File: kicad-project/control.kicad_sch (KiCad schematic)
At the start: 34 parts, among them J1 Conn_02x04_Counter_Clockwise, J2 Conn_02x08_Counter_Clockwise, SW1 HOME_SW, SW2 EN_SW, SW3 PRG_SW, SW4 RST_SW, U1 W25Q16JVSS, U2 RP2040, Y1 12MHz

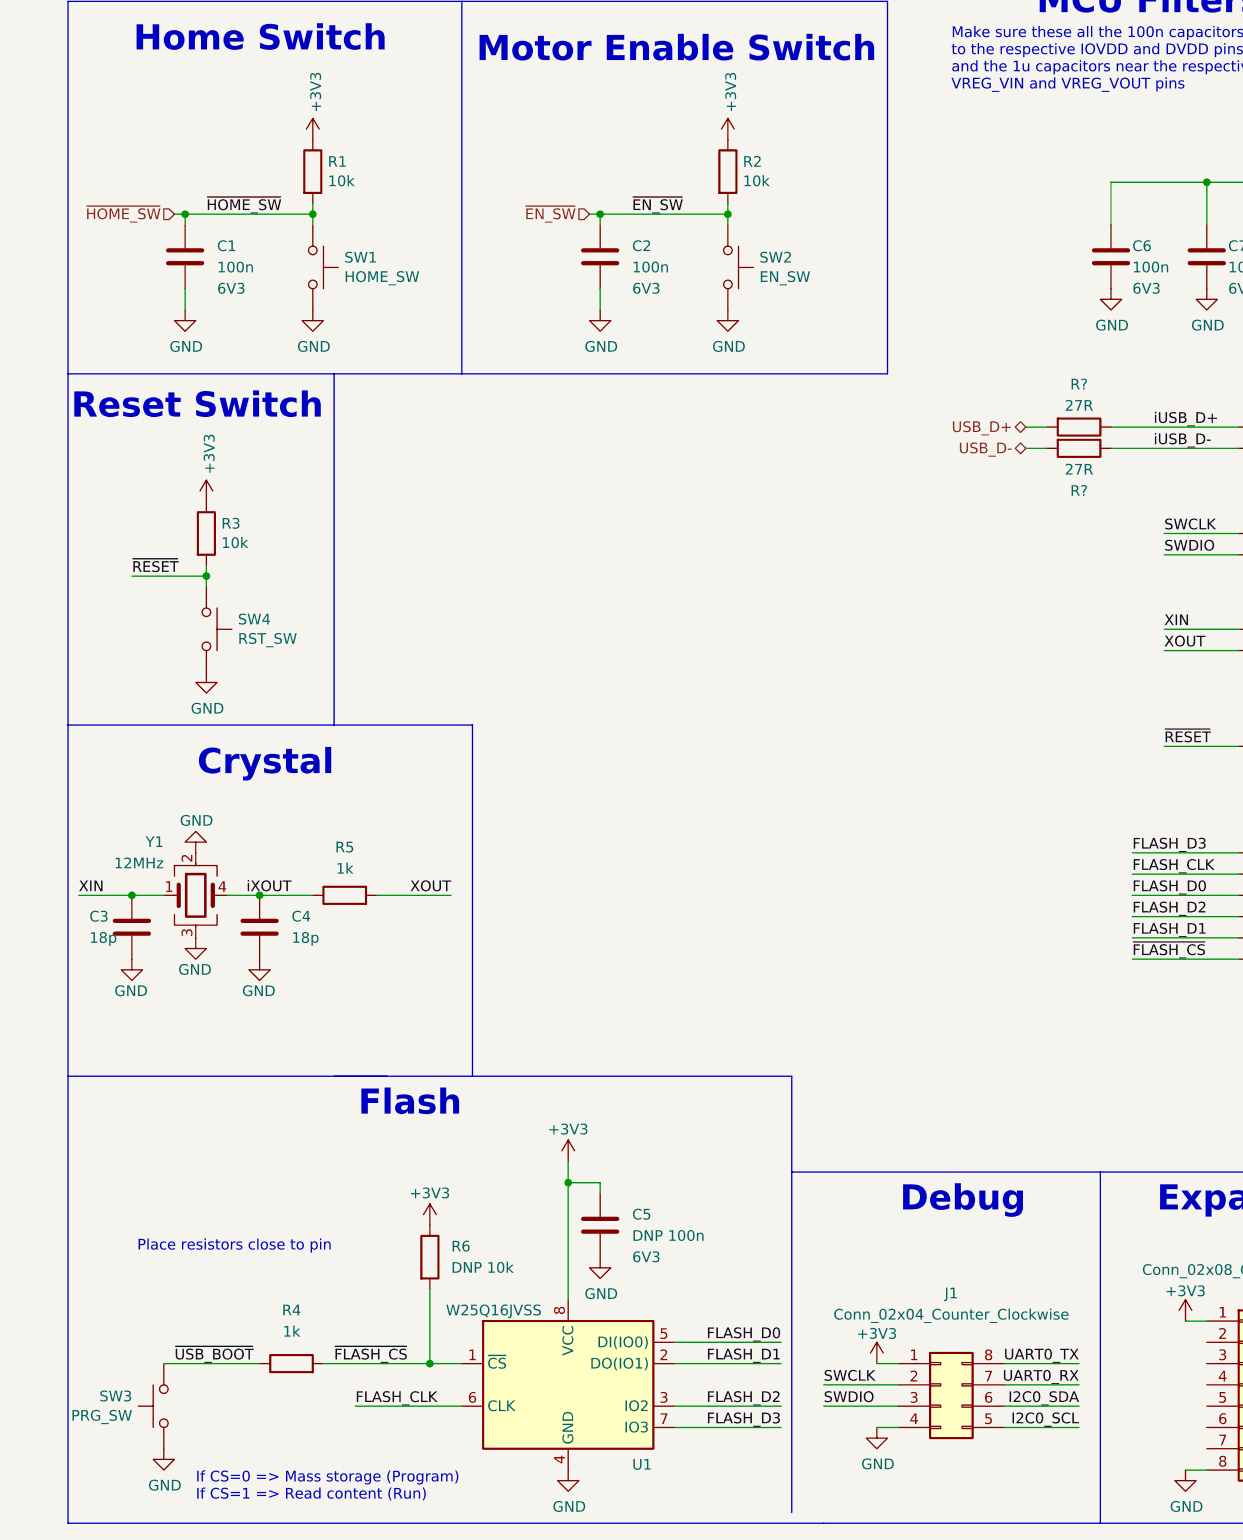
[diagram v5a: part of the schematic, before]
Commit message: hw: add mounting holes
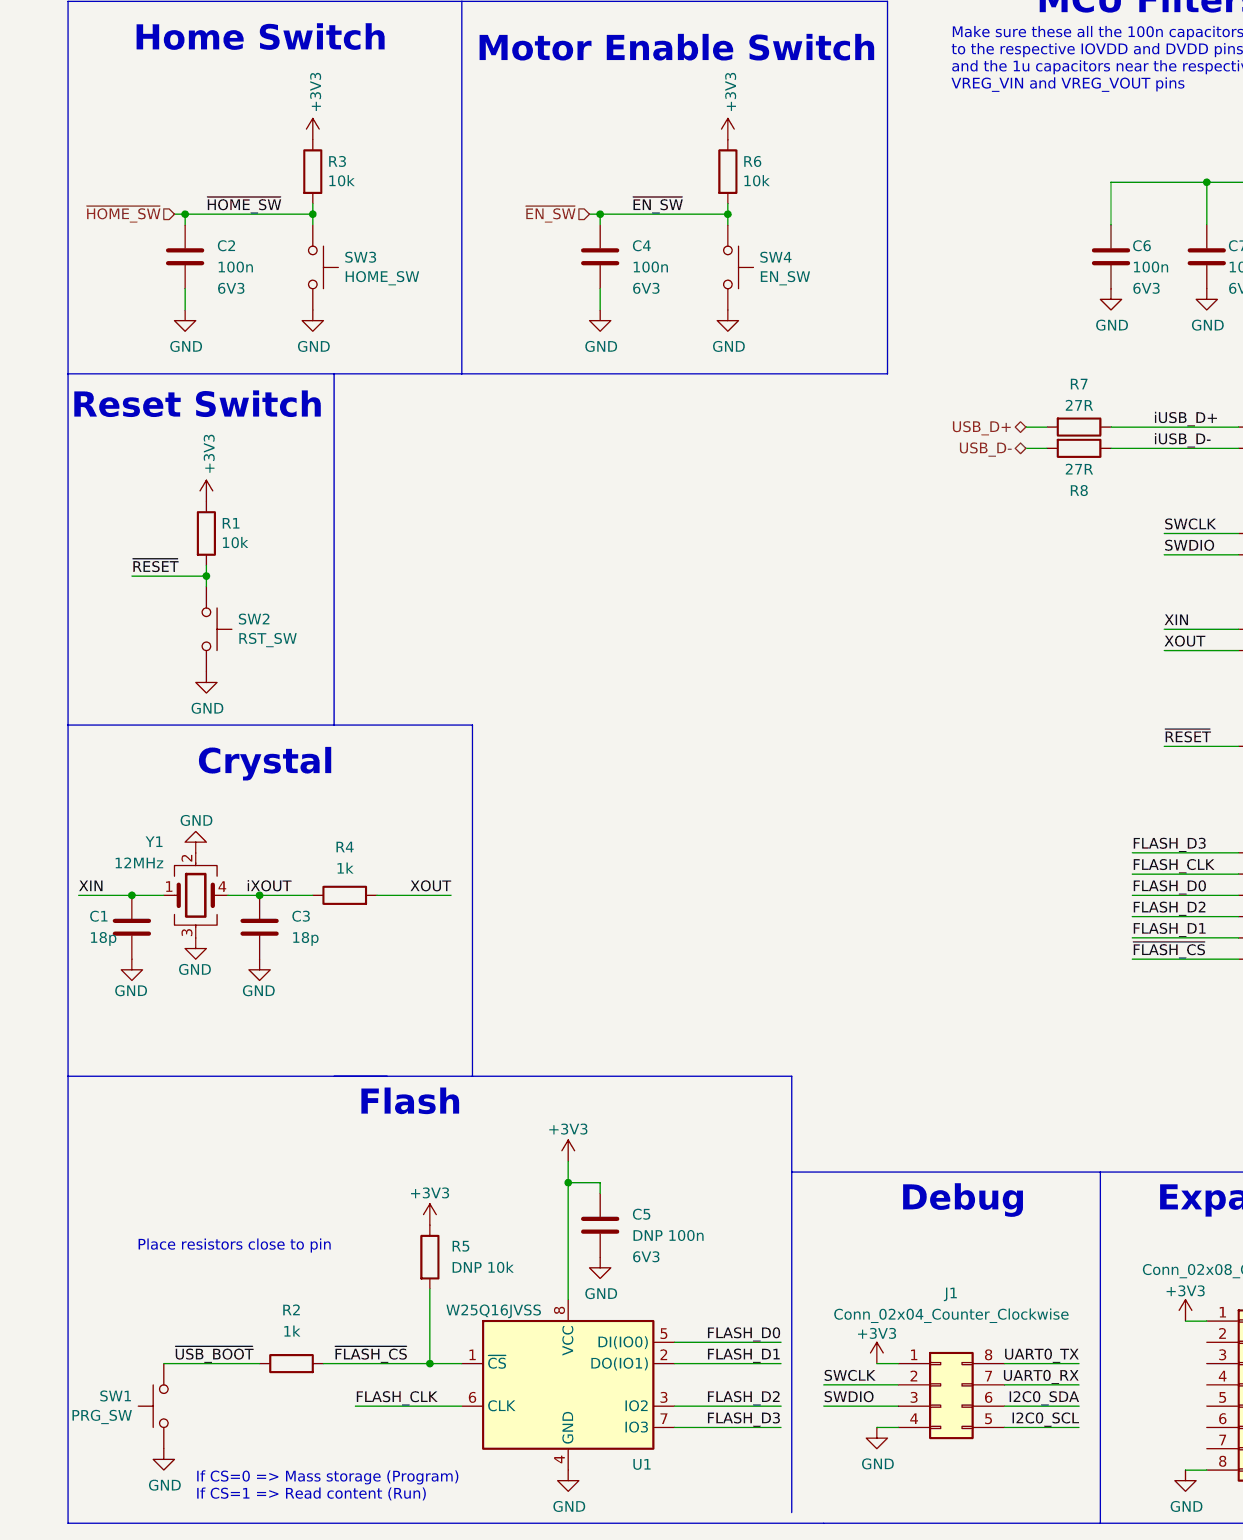
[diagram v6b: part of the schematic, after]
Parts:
- gave numbers to parts that had none: 2
- renumbered C3 to C1, C1 to C2, C4 to C3, C2 to C4, R3 to R1, R4 to R2, R1 to R3, R5 to R4, R6 to R5, R2 to R6, SW3 to SW1, SW4 to SW2, SW1 to SW3, SW2 to SW4
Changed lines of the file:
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@@
   (symbol (lib_id "Switch:SW_Push") (at 29.21 90.17 270) (unit 1)
     (in_bom yes) (on_board yes)
-    (property "Reference" "SW4" (id 0) (at 32.9692 89.0016 90)
+    (property "Reference" "SW2" (id 0) (at 32.9692 89.0016 90)
       (effects (font (size 1.27 1.27)) (justify left))
     )
@@
   (symbol (lib_id "Device:R") (at 29.21 78.74 0) (unit 1)
     (in_bom yes) (on_board yes)
-    (property "Reference" "R3" (id 0) (at 30.988 77.5716 0)
+    (property "Reference" "R1" (id 0) (at 30.988 77.5716 0)
       (effects (font (size 1.27 1.27)) (justify left))
     )
@@
   (symbol (lib_id "power:GND") (at 29.21 95.25 0) (unit 1)
     (in_bom yes) (on_board yes)
-    (property "Reference" "#PWR012" (id 0) (at 29.21 101.6 0)
+    (property "Reference" "#PWR07" (id 0) (at 29.21 101.6 0)
       (effects (font (size 1.27 1.27)) hide)
     )
@@
   (symbol (lib_id "power:+3V3") (at 29.21 74.93 0) (unit 1)
     (in_bom yes) (on_board yes)
-    (property "Reference" "#PWR011" (id 0) (at 29.21 78.74 0)
+    (property "Reference" "#PWR06" (id 0) (at 29.21 78.74 0)
       (effects (font (size 1.27 1.27)) hide)
     )
@@
   (symbol (lib_id "Device:R") (at 133.35 66.04 270) (unit 1)
     (in_bom yes) (on_board yes)
-    (property "Reference" "R?" (id 0) (at 133.35 60.96 90))
+    (property "Reference" "R7" (id 0) (at 133.35 60.96 90))
     (property "Value" "27R" (id 1) (at 133.35 63.5 90))
     (property "Footprint" "Resistor_SMD:R_0603_1608Metric" (id 2) (at 133.35 64.262 90)
@@
   (symbol (lib_id "Device:R") (at 133.35 68.58 270) (unit 1)
     (in_bom yes) (on_board yes)
-    (property "Reference" "R?" (id 0) (at 133.35 73.66 90))
+    (property "Reference" "R8" (id 0) (at 133.35 73.66 90))
     (property "Value" "27R" (id 1) (at 133.35 71.12 90))
     (property "Footprint" "Resistor_SMD:R_0603_1608Metric" (id 2) (at 133.35 66.802 90)
@@
   (symbol (lib_id "power:GND") (at 27.94 127 0) (unit 1)
     (in_bom yes) (on_board yes)
-    (property "Reference" "#PWR010" (id 0) (at 27.94 133.35 0)
+    (property "Reference" "#PWR05" (id 0) (at 27.94 133.35 0)
       (effects (font (size 1.27 1.27)) hide)
     )
@@
   (symbol (lib_id "power:GND") (at 27.94 116.84 180) (unit 1)
     (in_bom yes) (on_board yes)
-    (property "Reference" "#PWR09" (id 0) (at 27.94 110.49 0)
+    (property "Reference" "#PWR04" (id 0) (at 27.94 110.49 0)
       (effects (font (size 1.27 1.27)) hide)
     )
@@
   (symbol (lib_id "power:+3V3") (at 55.88 161.29 0) (unit 1)
     (in_bom yes) (on_board yes)
-    (property "Reference" "#PWR014" (id 0) (at 55.88 165.1 0)
+    (property "Reference" "#PWR011" (id 0) (at 55.88 165.1 0)
       (effects (font (size 1.27 1.27)) hide)
     )
@@
   (symbol (lib_id "Device:R") (at 91.44 35.56 0) (unit 1)
     (in_bom yes) (on_board yes)
-    (property "Reference" "R2" (id 0) (at 93.218 34.3916 0)
+    (property "Reference" "R6" (id 0) (at 93.218 34.3916 0)
       (effects (font (size 1.27 1.27)) (justify left))
     )
@@
   (symbol (lib_id "power:GND") (at 24.13 187.96 0) (unit 1)
     (in_bom yes) (on_board yes)
-    (property "Reference" "#PWR08" (id 0) (at 24.13 194.31 0)
+    (property "Reference" "#PWR02" (id 0) (at 24.13 194.31 0)
       (effects (font (size 1.27 1.27)) hide)
     )
@@
   (symbol (lib_id "Switch:SW_Push") (at 91.44 46.99 270) (unit 1)
     (in_bom yes) (on_board yes)
-    (property "Reference" "SW2" (id 0) (at 95.1992 45.8216 90)
+    (property "Reference" "SW4" (id 0) (at 95.1992 45.8216 90)
       (effects (font (size 1.27 1.27)) (justify left))
     )
@@
   (symbol (lib_id "Switch:SW_Push") (at 24.13 182.88 90) (mirror x) (unit 1)
     (in_bom yes) (on_board yes)
-    (property "Reference" "SW3" (id 0) (at 20.3708 181.7116 90)
+    (property "Reference" "SW1" (id 0) (at 20.3708 181.7116 90)
       (effects (font (size 1.27 1.27)) (justify left))
     )
@@
   (symbol (lib_id "power:GND") (at 76.2 165.1 0) (unit 1)
     (in_bom yes) (on_board yes)
-    (property "Reference" "#PWR017" (id 0) (at 76.2 171.45 0)
+    (property "Reference" "#PWR015" (id 0) (at 76.2 171.45 0)
       (effects (font (size 1.27 1.27)) hide)
     )
@@
   (symbol (lib_id "Device:C") (at 76.2 45.72 0) (unit 1)
     (in_bom yes) (on_board yes)
-    (property "Reference" "C2" (id 0) (at 80.01 44.4499 0)
+    (property "Reference" "C4" (id 0) (at 80.01 44.4499 0)
       (effects (font (size 1.27 1.27)) (justify left))
     )
@@
   (symbol (lib_id "Device:C") (at 20.32 125.73 0) (unit 1)
     (in_bom yes) (on_board yes)
-    (property "Reference" "C3" (id 0) (at 15.24 124.46 0)
+    (property "Reference" "C1" (id 0) (at 15.24 124.46 0)
       (effects (font (size 1.27 1.27)) (justify left))
     )
@@
   (symbol (lib_id "Device:C") (at 26.67 45.72 0) (unit 1)
     (in_bom yes) (on_board yes)
-    (property "Reference" "C1" (id 0) (at 30.48 44.4499 0)
+    (property "Reference" "C2" (id 0) (at 30.48 44.4499 0)
       (effects (font (size 1.27 1.27)) (justify left))
     )
@@
   (symbol (lib_id "Device:C") (at 35.56 125.73 0) (unit 1)
     (in_bom yes) (on_board yes) (fields_autoplaced)
-    (property "Reference" "C4" (id 0) (at 39.37 124.4599 0)
+    (property "Reference" "C3" (id 0) (at 39.37 124.4599 0)
       (effects (font (size 1.27 1.27)) (justify left))
     )
@@
   (symbol (lib_id "Device:R") (at 39.37 177.8 90) (unit 1)
     (in_bom yes) (on_board yes) (fields_autoplaced)
-    (property "Reference" "R4" (id 0) (at 39.37 171.45 90))
+    (property "Reference" "R2" (id 0) (at 39.37 171.45 90))
     (property "Value" "1k" (id 1) (at 39.37 173.99 90))
     (property "Footprint" "Resistor_SMD:R_0603_1608Metric" (id 2) (at 39.37 179.578 90)
@@
   (symbol (lib_id "power:GND") (at 41.91 52.07 0) (unit 1)
     (in_bom yes) (on_board yes)
-    (property "Reference" "#PWR03" (id 0) (at 41.91 58.42 0)
+    (property "Reference" "#PWR010" (id 0) (at 41.91 58.42 0)
       (effects (font (size 1.27 1.27)) hide)
     )
@@
   (symbol (lib_id "Switch:SW_Push") (at 41.91 46.99 270) (unit 1)
     (in_bom yes) (on_board yes)
-    (property "Reference" "SW1" (id 0) (at 45.6692 45.8216 90)
+    (property "Reference" "SW3" (id 0) (at 45.6692 45.8216 90)
       (effects (font (size 1.27 1.27)) (justify left))
     )
@@
   (symbol (lib_id "power:+3V3") (at 41.91 31.75 0) (unit 1)
     (in_bom yes) (on_board yes)
-    (property "Reference" "#PWR02" (id 0) (at 41.91 35.56 0)
+    (property "Reference" "#PWR09" (id 0) (at 41.91 35.56 0)
       (effects (font (size 1.27 1.27)) hide)
     )
@@
   (symbol (lib_id "Device:R") (at 41.91 35.56 0) (unit 1)
     (in_bom yes) (on_board yes)
-    (property "Reference" "R1" (id 0) (at 43.688 34.3916 0)
+    (property "Reference" "R3" (id 0) (at 43.688 34.3916 0)
       (effects (font (size 1.27 1.27)) (justify left))
     )
@@
   (symbol (lib_id "power:GND") (at 72.39 190.5 0) (unit 1)
     (in_bom yes) (on_board yes)
-    (property "Reference" "#PWR016" (id 0) (at 72.39 196.85 0)
+    (property "Reference" "#PWR013" (id 0) (at 72.39 196.85 0)
       (effects (font (size 1.27 1.27)) hide)
     )
@@
   (symbol (lib_id "power:GND") (at 26.67 52.07 0) (unit 1)
     (in_bom yes) (on_board yes)
-    (property "Reference" "#PWR01" (id 0) (at 26.67 58.42 0)
+    (property "Reference" "#PWR03" (id 0) (at 26.67 58.42 0)
       (effects (font (size 1.27 1.27)) hide)
     )
@@
   (symbol (lib_id "Device:R") (at 45.72 121.92 90) (unit 1)
     (in_bom yes) (on_board yes) (fields_autoplaced)
-    (property "Reference" "R5" (id 0) (at 45.72 116.205 90))
+    (property "Reference" "R4" (id 0) (at 45.72 116.205 90))
     (property "Value" "1k" (id 1) (at 45.72 118.745 90))
     (property "Footprint" "Resistor_SMD:R_0603_1608Metric" (id 2) (at 45.72 123.698 90)
@@
   (symbol (lib_id "power:GND") (at 20.32 129.54 0) (unit 1)
     (in_bom yes) (on_board yes)
-    (property "Reference" "#PWR07" (id 0) (at 20.32 135.89 0)
+    (property "Reference" "#PWR01" (id 0) (at 20.32 135.89 0)
       (effects (font (size 1.27 1.27)) hide)
     )
@@
   (symbol (lib_id "power:GND") (at 91.44 52.07 0) (unit 1)
     (in_bom yes) (on_board yes)
-    (property "Reference" "#PWR06" (id 0) (at 91.44 58.42 0)
+    (property "Reference" "#PWR017" (id 0) (at 91.44 58.42 0)
       (effects (font (size 1.27 1.27)) hide)
     )
@@
   (symbol (lib_id "power:+3V3") (at 72.39 153.67 0) (unit 1)
     (in_bom yes) (on_board yes)
-    (property "Reference" "#PWR015" (id 0) (at 72.39 157.48 0)
+    (property "Reference" "#PWR012" (id 0) (at 72.39 157.48 0)
       (effects (font (size 1.27 1.27)) hide)
     )
@@
   (symbol (lib_id "power:GND") (at 35.56 129.54 0) (unit 1)
     (in_bom yes) (on_board yes)
-    (property "Reference" "#PWR013" (id 0) (at 35.56 135.89 0)
+    (property "Reference" "#PWR08" (id 0) (at 35.56 135.89 0)
       (effects (font (size 1.27 1.27)) hide)
     )
@@
   (symbol (lib_id "power:+3V3") (at 91.44 31.75 0) (unit 1)
     (in_bom yes) (on_board yes)
-    (property "Reference" "#PWR05" (id 0) (at 91.44 35.56 0)
+    (property "Reference" "#PWR016" (id 0) (at 91.44 35.56 0)
       (effects (font (size 1.27 1.27)) hide)
     )
@@
   (symbol (lib_id "Device:R") (at 55.88 165.1 0) (unit 1)
     (in_bom yes) (on_board yes) (fields_autoplaced)
-    (property "Reference" "R6" (id 0) (at 58.42 163.8299 0)
+    (property "Reference" "R5" (id 0) (at 58.42 163.8299 0)
       (effects (font (size 1.27 1.27)) (justify left))
     )
@@
   (symbol (lib_id "power:GND") (at 76.2 52.07 0) (unit 1)
     (in_bom yes) (on_board yes)
-    (property "Reference" "#PWR04" (id 0) (at 76.2 58.42 0)
-      (effects (font (size 1.27 1.27)) hide)
-    )
+    (property "Reference" "#PWR014" (id 0) (at 76.2 58.42 0)
+      (effects (font (size 1.27 1.27)) hide)
+    )

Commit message: hw: first layout draft
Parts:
- J1: footprint Connector_PinHeader_2.54mm:PinHeader_2x04_P2.54mm_Vertical_SMD -> Connector_PinHeader_2.54mm:PinHeader_2x04_P2.54mm_Vertical
- J2: footprint Connector_PinHeader_2.54mm:PinHeader_2x08_P2.54mm_Vertical_SMD -> Connector_PinHeader_2.54mm:PinHeader_2x08_P2.54mm_Vertical
- U2: footprint AA_PPSE_2021:RP2040-Hand-Solder -> ppse_2021:RP2040-Hand-Solder
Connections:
- net GPIO23: now reaches U2.35 (GPIO23)
- net GPIO24: now reaches U2.36 (GPIO24)
- net GPIO25: now reaches U2.37 (GPIO25)
- net GPIO6: now reaches U2.8 (GPIO6)
- net I2C1_SCL renamed ACC_INT
- net I2C1_SDA renamed CMP_DRDY
- no-connect marks 3 -> 0
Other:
- note added: "Make sure to place all capacitors close to their respective pins"
- note removed: "Make sure these all the 100n capacitors close to the respective IOVDD and DVDD pins and the 1u capacitors near the respective VREG_VIN and VREG_VOUT pins"
- moved on the sheet: C10, C11, C12, C13, C14, C15, C16, C17, C2, C4, C6, C7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

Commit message: hw: classroom changes
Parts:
- removed Y1: 12MHz, Crystal:Crystal_SMD_3225-4Pin_3.2x2.5mm, symbol Device:Crystal_GND23
- added Y1: 12MHz, Crystal:Crystal_SMD_3225-4Pin_3.2x2.5mm, symbol Device:Crystal_GND24
- J2: footprint Connector_PinHeader_2.54mm:PinHeader_2x08_P2.54mm_Vertical -> Connector_PinHeader_2.54mm:PinHeader_2x05_P2.54mm_Vertical; symbol Connector_Generic:Conn_02x08_Counter_Clockwise -> Connector_Generic:Conn_02x05_Counter_Clockwise
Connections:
- net EXT_ADC0: now also J2.8 (Pin_8); no longer J2.10 (Pin_10)
- net EXT_ADC1: now also J2.7 (Pin_7); no longer J2.9 (Pin_9)
- net GND: now also J2.6 (Pin_6), Y1.2, Y1.4; no longer J2.8 (Pin_8)
- net GPIO23: now also J2.3 (Pin_3)
- net GPIO24: now also J2.4 (Pin_4)
- net GPIO25: now also J2.5 (Pin_5)
- net GPIO6: now also J2.2 (Pin_2)
- net I2C0_SCL: now also J2.9 (Pin_9); no longer J2.11 (Pin_11)
- net I2C0_SDA: now also J2.10 (Pin_10); no longer J2.12 (Pin_12)
- net XIN: now also Y1.1
- net iXOUT: now also Y1.3
